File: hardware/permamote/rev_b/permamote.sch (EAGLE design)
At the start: 130 parts, among them J1 TC2030-JLINK-NL, J5 MICRO_USB_B_HIROSE_ZX62R-B-5P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, Q1 PMDXB950UPEL, Q10 PMDXB950UPEL, Q2 PMDXB950UPEL, Q3 PMDXB950UPEL, Q4 PMDXB950UPEL, Q5 PMDXB950UPEL, Q6 PMDXB950UPEL, Q7 PMDXB950UPEL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

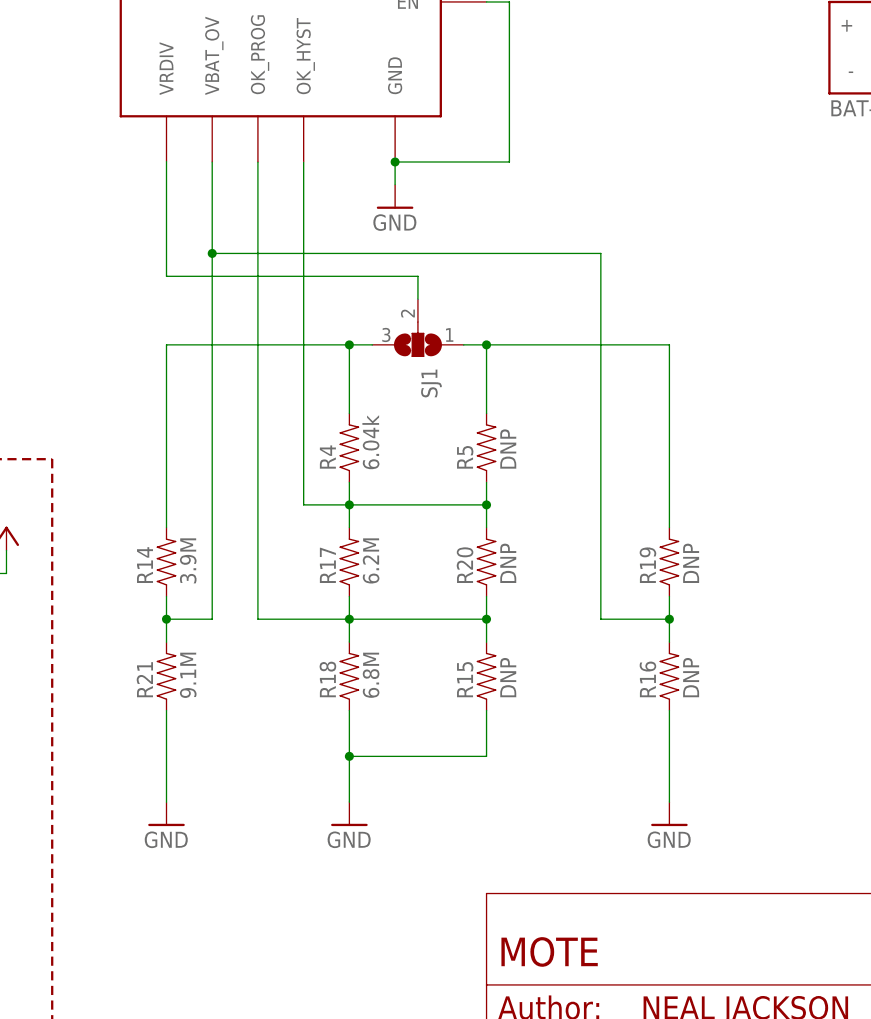
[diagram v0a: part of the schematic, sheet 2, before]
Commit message: Move coin cell holder out from under PIR
Move button/led to debug edge of board
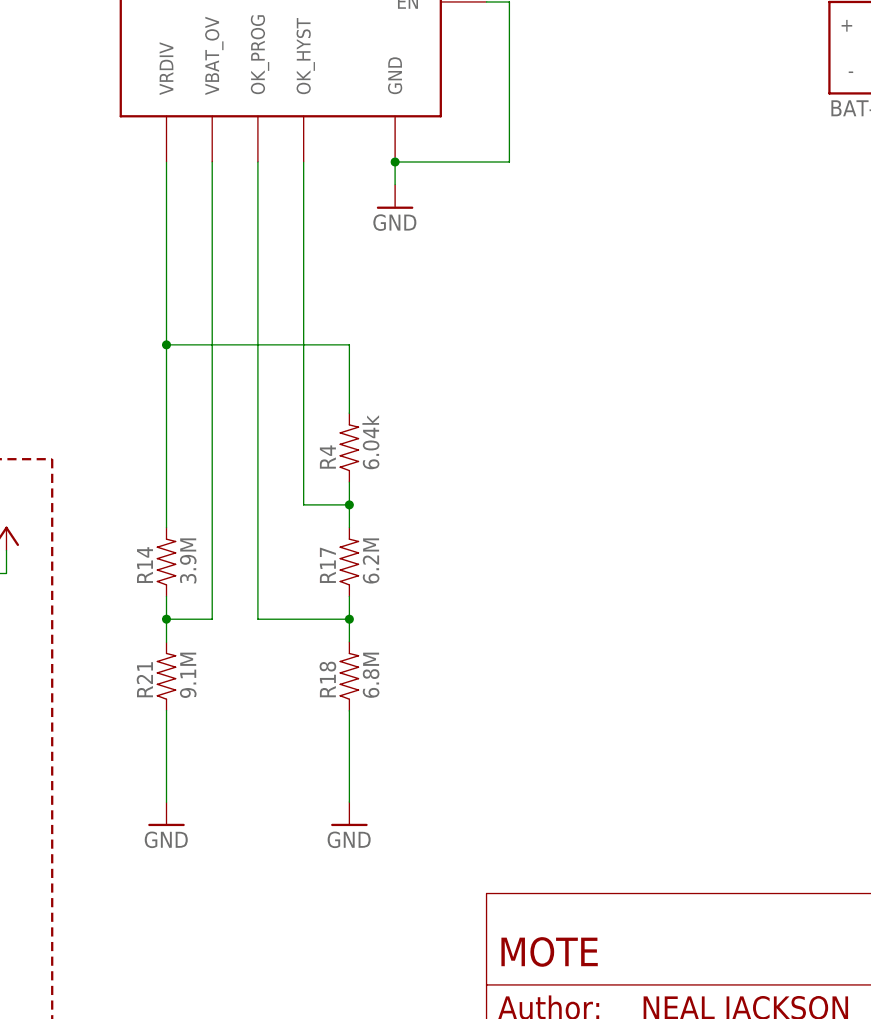
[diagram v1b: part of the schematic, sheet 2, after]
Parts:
- removed R15, R16, R19, R20, R5: DNP, passives:RESISTOR0402_RES
- removed SJ1: (no value), jumper:SJ2W
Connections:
- removed net N$1: R14.2, R4.2, SJ1.3
- removed net N$16: R19.2, R5.2, SJ1.1
- net GND: no longer R15.1, R16.1
- net N$18: no longer R16.2, R19.1
- net N$32: now also R14.2, R4.2; no longer SJ1.2
- net N$57: no longer R15.2, R20.1
- net N$58: no longer R20.2, R5.1
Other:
- note removed: "Divider for Other"
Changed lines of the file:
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@@
 <part name="GND23" library="supply1" library_urn="urn:adsk.eagle:library:371" deviceset="GND" device=""/>
 <part name="GND19" library="supply1" library_urn="urn:adsk.eagle:library:371" deviceset="GND" device=""/>
-<part name="SJ1" library="jumper" library_urn="urn:adsk.eagle:library:252" deviceset="SJ2W" device="" package3d_urn="urn:adsk.eagle:package:15474/1"/>
-<part name="R5" library="passives" deviceset="RESISTOR" device="0402_RES" value="DNP">
-<attribute name="DIGIKEY" value="YAG3306CT-ND"/>
-</part>
-<part name="R20" library="passives" deviceset="RESISTOR" device="0402_RES" value="DNP">
-<attribute name="DIGIKEY" value="YAG3306CT-ND"/>
-</part>
-<part name="R15" library="passives" deviceset="RESISTOR" device="0402_RES" value="DNP">
-<attribute name="DIGIKEY" value="YAG3306CT-ND"/>
-</part>
 <part name="BT2" library="batteries" deviceset="BAT-HLD-002-THM" device="">
 <attribute name="DIGIKEY" value="BAT-HLD-001-THM-ND"/>
@@
 <attribute name="MPN" value="BAT-HLD-001-THM"/>
 </part>
-<part name="R19" library="passives" deviceset="RESISTOR" device="0402_RES" value="DNP">
-<attribute name="DIGIKEY" value="YAG3306CT-ND"/>
-</part>
-<part name="R16" library="passives" deviceset="RESISTOR" device="0402_RES" value="DNP">
-<attribute name="DIGIKEY" value="YAG3306CT-ND"/>
-</part>
-<part name="GND31" library="supply1" library_urn="urn:adsk.eagle:library:371" deviceset="GND" device=""/>
 <part name="L3" library="passives" deviceset="INDUCTOR" device="IHL" value="1uH">
 <attribute name="DIGIKEY" value="541-1319-1-ND"/>
@@
 <text x="2.54" y="66.04" size="2.54" layer="97">Boost Regulator</text>
 <text x="124.46" y="53.34" size="1.778" layer="98" rot="R90" align="bottom-center">Divider for Lithium Titanate</text>
-<text x="162.56" y="53.34" size="1.778" layer="98" rot="R90" align="bottom-center">Divider for Other</text>
 </plain>
 <instances>
@@
 <instance part="GND23" gate="1" x="142.24" y="96.52"/>
 <instance part="GND19" gate="1" x="215.9" y="134.62"/>
-<instance part="SJ1" gate="G$1" x="144.78" y="81.28" rot="R270"/>
-<instance part="R5" gate="G$1" x="152.4" y="71.12" rot="R90">
-<attribute name="DIGIKEY" x="152.4" y="71.12" size="1.778" layer="96" rot="R90" display="off"/>
-</instance>
-<instance part="R20" gate="G$1" x="152.4" y="58.42" rot="R90">
-<attribute name="DIGIKEY" x="152.4" y="58.42" size="1.778" layer="96" rot="R90" display="off"/>
-</instance>
-<instance part="R15" gate="G$1" x="152.4" y="45.72" rot="R90">
-<attribute name="DIGIKEY" x="152.4" y="45.72" size="1.778" layer="96" rot="R90" display="off"/>
-</instance>
 <instance part="BT2" gate="G$1" x="193.04" y="114.3">
 <attribute name="MPN" x="193.04" y="114.3" size="1.778" layer="96" display="off"/>
@@
 <attribute name="MPN" x="215.9" y="114.3" size="1.778" layer="96" display="off"/>
 </instance>
-<instance part="R19" gate="G$1" x="172.72" y="58.42" rot="R90">
-<attribute name="DIGIKEY" x="172.72" y="58.42" size="1.778" layer="96" rot="R90" display="off"/>
-</instance>
-<instance part="R16" gate="G$1" x="172.72" y="45.72" rot="R90">
-<attribute name="DIGIKEY" x="172.72" y="45.72" size="1.778" layer="96" rot="R90" display="off"/>
-</instance>
-<instance part="GND31" gate="1" x="172.72" y="27.94"/>
 <instance part="L3" gate="G$1" x="48.26" y="63.5" rot="R90"/>
 <instance part="GND4" gate="1" x="124.46" y="165.1"/>
@@
 <pinref part="GND22" gate="1" pin="GND"/>
 <pinref part="R18" gate="G$1" pin="1"/>
-<wire x1="137.16" y1="30.48" x2="137.16" y2="35.56" width="0.1524" layer="91"/>
-<pinref part="R15" gate="G$1" pin="1"/>
-<wire x1="137.16" y1="35.56" x2="137.16" y2="40.64" width="0.1524" layer="91"/>
-<wire x1="152.4" y1="40.64" x2="152.4" y2="35.56" width="0.1524" layer="91"/>
-<wire x1="152.4" y1="35.56" x2="137.16" y2="35.56" width="0.1524" layer="91"/>
-<junction x="137.16" y="35.56"/>
+<wire x1="137.16" y1="30.48" x2="137.16" y2="40.64" width="0.1524" layer="91"/>
 </segment>
 <segment>
@@
 <pinref part="BT1" gate="G$1" pin="-"/>
 <wire x1="215.9" y1="137.16" x2="215.9" y2="139.7" width="0.1524" layer="91"/>
-</segment>
-<segment>
-<pinref part="GND31" gate="1" pin="GND"/>
-<pinref part="R16" gate="G$1" pin="1"/>
-<wire x1="172.72" y1="30.48" x2="172.72" y2="40.64" width="0.1524" layer="91"/>
 </segment>
 <segment>
@@
 <junction x="116.84" y="50.8"/>
 <pinref part="U2" gate="G$1" pin="VBAT_OV"/>
-<wire x1="121.92" y1="50.8" x2="121.92" y2="91.44" width="0.1524" layer="91"/>
-<wire x1="121.92" y1="91.44" x2="121.92" y2="101.6" width="0.1524" layer="91"/>
-<wire x1="121.92" y1="91.44" x2="165.1" y2="91.44" width="0.1524" layer="91"/>
-<junction x="121.92" y="91.44"/>
-<wire x1="165.1" y1="91.44" x2="165.1" y2="50.8" width="0.1524" layer="91"/>
-<pinref part="R16" gate="G$1" pin="2"/>
-<pinref part="R19" gate="G$1" pin="1"/>
-<wire x1="172.72" y1="48.26" x2="172.72" y2="50.8" width="0.1524" layer="91"/>
-<wire x1="172.72" y1="50.8" x2="172.72" y2="53.34" width="0.1524" layer="91"/>
-<wire x1="165.1" y1="50.8" x2="172.72" y2="50.8" width="0.1524" layer="91"/>
-<junction x="172.72" y="50.8"/>
+<wire x1="121.92" y1="50.8" x2="121.92" y2="101.6" width="0.1524" layer="91"/>
 </segment>
 </net>
@@
 <segment>
 <pinref part="U2" gate="G$1" pin="VRDIV"/>
-<wire x1="116.84" y1="88.9" x2="116.84" y2="101.6" width="0.1524" layer="91"/>
-<wire x1="116.84" y1="88.9" x2="144.78" y2="88.9" width="0.1524" layer="91"/>
-<pinref part="SJ1" gate="G$1" pin="2"/>
-<wire x1="144.78" y1="88.9" x2="144.78" y2="86.36" width="0.1524" layer="91"/>
+<wire x1="116.84" y1="81.28" x2="116.84" y2="101.6" width="0.1524" layer="91"/>
+<pinref part="R4" gate="G$1" pin="2"/>
+<wire x1="137.16" y1="81.28" x2="137.16" y2="73.66" width="0.1524" layer="91"/>
+<wire x1="137.16" y1="81.28" x2="116.84" y2="81.28" width="0.1524" layer="91"/>
+<pinref part="R14" gate="G$1" pin="2"/>
+<wire x1="116.84" y1="81.28" x2="116.84" y2="60.96" width="0.1524" layer="91"/>
+<junction x="116.84" y="81.28"/>
 </segment>
 </net>
@@
 <wire x1="127" y1="50.8" x2="137.16" y2="50.8" width="0.1524" layer="91"/>
 <junction x="137.16" y="50.8"/>
-<pinref part="R15" gate="G$1" pin="2"/>
-<pinref part="R20" gate="G$1" pin="1"/>
-<wire x1="152.4" y1="48.26" x2="152.4" y2="50.8" width="0.1524" layer="91"/>
-<wire x1="152.4" y1="50.8" x2="152.4" y2="53.34" width="0.1524" layer="91"/>
-<wire x1="137.16" y1="50.8" x2="152.4" y2="50.8" width="0.1524" layer="91"/>
-<junction x="152.4" y="50.8"/>
 </segment>
 </net>
@@
 <wire x1="132.08" y1="63.5" x2="137.16" y2="63.5" width="0.1524" layer="91"/>
 <junction x="137.16" y="63.5"/>
-<pinref part="R20" gate="G$1" pin="2"/>
-<pinref part="R5" gate="G$1" pin="1"/>
-<wire x1="152.4" y1="60.96" x2="152.4" y2="63.5" width="0.1524" layer="91"/>
-<wire x1="152.4" y1="63.5" x2="152.4" y2="66.04" width="0.1524" layer="91"/>
-<wire x1="137.16" y1="63.5" x2="152.4" y2="63.5" width="0.1524" layer="91"/>
-<junction x="152.4" y="63.5"/>
-</segment>
-</net>
-<net name="N$1" class="0">
-<segment>
-<pinref part="SJ1" gate="G$1" pin="3"/>
-<wire x1="139.7" y1="81.28" x2="137.16" y2="81.28" width="0.1524" layer="91"/>
-<pinref part="R4" gate="G$1" pin="2"/>
-<wire x1="137.16" y1="81.28" x2="137.16" y2="73.66" width="0.1524" layer="91"/>
-<wire x1="137.16" y1="81.28" x2="116.84" y2="81.28" width="0.1524" layer="91"/>
-<junction x="137.16" y="81.28"/>
-<pinref part="R14" gate="G$1" pin="2"/>
-<wire x1="116.84" y1="81.28" x2="116.84" y2="60.96" width="0.1524" layer="91"/>
-</segment>
-</net>
-<net name="N$16" class="0">
-<segment>
-<pinref part="R5" gate="G$1" pin="2"/>
-<wire x1="152.4" y1="73.66" x2="152.4" y2="81.28" width="0.1524" layer="91"/>
-<pinref part="SJ1" gate="G$1" pin="1"/>
-<wire x1="152.4" y1="81.28" x2="149.86" y2="81.28" width="0.1524" layer="91"/>
-<pinref part="R19" gate="G$1" pin="2"/>
-<wire x1="172.72" y1="60.96" x2="172.72" y2="81.28" width="0.1524" layer="91"/>
-<wire x1="172.72" y1="81.28" x2="152.4" y2="81.28" width="0.1524" layer="91"/>
-<junction x="152.4" y="81.28"/>
-</segment>
-</net>
+</segment>
+</net>

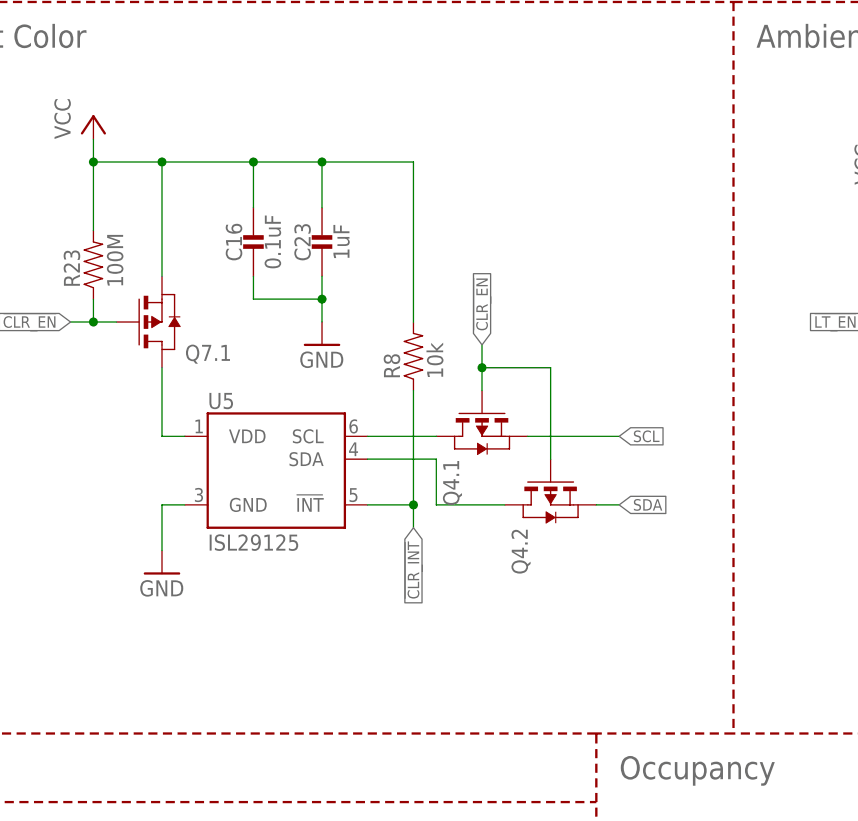
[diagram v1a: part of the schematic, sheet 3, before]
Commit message: Switch to TCS34725 color sensor
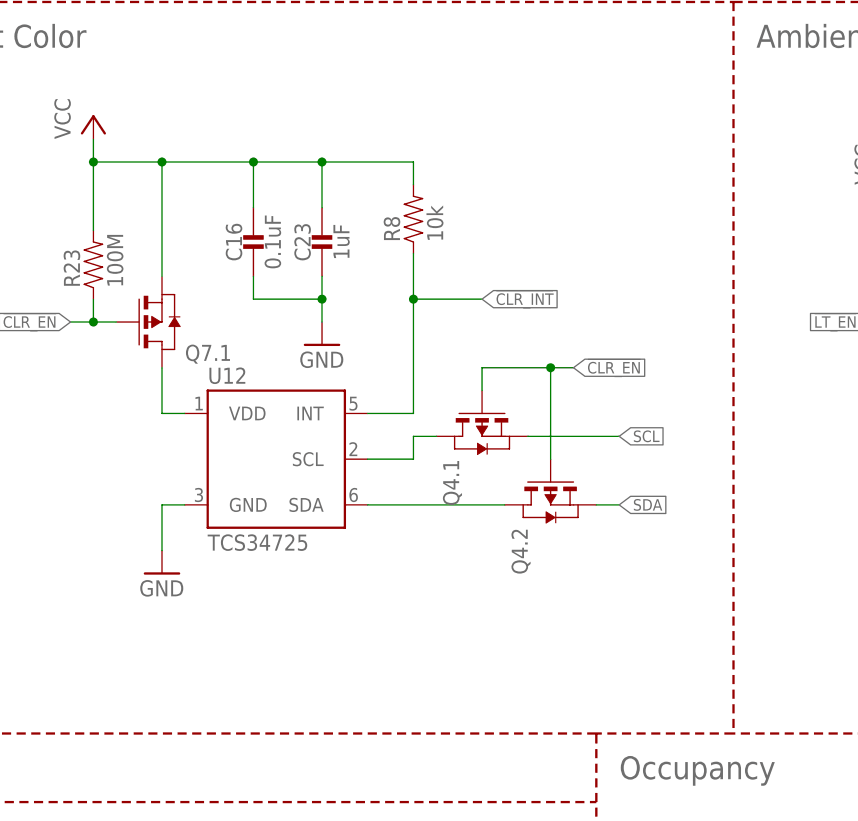
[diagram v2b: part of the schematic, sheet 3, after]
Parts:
- removed U5: ISL29125, chips:ISL29125
- added U12: TCS34725, chips:TCS34725
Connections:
- net !CLR_INT: now also U12.INT; no longer U5.!INT
- net GND: now also U12.GND; no longer U5.GND
- net N$31: now also U12.VDD; no longer U5.VDD
- net N$54: now also U12.SDA; no longer U5.SDA
- net N$55: now also U12.SCL; no longer U5.SCL
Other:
- moved on the sheet: R8
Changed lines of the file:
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@@
 <?xml version="1.0" encoding="utf-8"?>
 <!DOCTYPE eagle SYSTEM "eagle.dtd">
-<eagle version="9.0.0">
+<eagle version="9.0.1">
 <drawing>
 <settings>
@@
 <part name="P+4" library="mote" deviceset="VBAT" device=""/>
 <part name="FRAME3" library="lab11-frames" deviceset="LETTER_L_BLANK" device=""/>
-<part name="U5" library="chips" deviceset="ISL29125" device=""/>
 <part name="U8" library="chips" deviceset="MAX44009" device=""/>
 <part name="C23" library="passives" deviceset="CAPACITOR" device="0402_CAP" value="1uF">
@@
 <part name="TP26" library="headers" deviceset="TEST-POINT" device=""/>
 <part name="TP27" library="headers" deviceset="TEST-POINT" device=""/>
+<part name="U12" library="chips" deviceset="TCS34725" device=""/>
 </parts>
 <sheets>
@@
 <instance part="FRAME3" gate="G$1" x="0" y="0"/>
 <instance part="FRAME3" gate="G$2" x="152.4" y="0"/>
-<instance part="U5" gate="G$1" x="109.22" y="111.76"/>
 <instance part="U8" gate="G$1" x="195.58" y="111.76"/>
 <instance part="C23" gate="G$1" x="121.92" y="144.78">
@@
 <instance part="GND26" gate="1" x="35.56" y="38.1"/>
 <instance part="GND27" gate="1" x="114.3" y="38.1"/>
-<instance part="R8" gate="G$1" x="132.08" y="132.08" rot="R90">
-<attribute name="DIGIKEY" x="132.08" y="132.08" size="1.778" layer="96" rot="R90" display="off"/>
-<attribute name="MPN" x="132.08" y="132.08" size="1.778" layer="96" rot="R90" display="off"/>
+<instance part="R8" gate="G$1" x="132.08" y="147.32" rot="R90">
+<attribute name="DIGIKEY" x="132.08" y="147.32" size="1.778" layer="96" rot="R90" display="off"/>
+<attribute name="MPN" x="132.08" y="147.32" size="1.778" layer="96" rot="R90" display="off"/>
 </instance>
 <instance part="R9" gate="G$1" x="220.98" y="137.16" rot="R90">
@@
 <instance part="Q8" gate=".2" x="93.98" y="45.72" rot="MR180"/>
 <instance part="Q10" gate=".1" x="180.34" y="50.8" rot="MR180"/>
+<instance part="U12" gate="G$1" x="109.22" y="111.76"/>
 </instances>
 <busses>
@@
 <net name="GND" class="0">
 <segment>
-<pinref part="U5" gate="G$1" pin="GND"/>
-<wire x1="106.68" y1="114.3" x2="104.14" y2="114.3" width="0.1524" layer="91"/>
 <pinref part="GND11" gate="1" pin="GND"/>
 <wire x1="104.14" y1="114.3" x2="104.14" y2="109.22" width="0.1524" layer="91"/>
+<pinref part="U12" gate="G$1" pin="GND"/>
+<wire x1="104.14" y1="114.3" x2="106.68" y2="114.3" width="0.1524" layer="91"/>
 </segment>
 <segment>
@@
 <junction x="121.92" y="152.4"/>
 <pinref part="R8" gate="G$1" pin="2"/>
-<wire x1="132.08" y1="134.62" x2="132.08" y2="152.4" width="0.1524" layer="91"/>
+<wire x1="132.08" y1="149.86" x2="132.08" y2="152.4" width="0.1524" layer="91"/>
 <pinref part="P+6" gate="VCC" pin="VCC"/>
 <wire x1="96.52" y1="154.94" x2="96.52" y2="152.4" width="0.1524" layer="91"/>
@@
 <net name="!CLR_INT" class="0">
 <segment>
-<pinref part="U5" gate="G$1" pin="!INT"/>
-<wire x1="127" y1="114.3" x2="132.08" y2="114.3" width="0.1524" layer="91"/>
-<label x="132.08" y="111.76" size="1.27" layer="95" rot="R270" xref="yes"/>
 <pinref part="R8" gate="G$1" pin="1"/>
-<wire x1="132.08" y1="114.3" x2="132.08" y2="111.76" width="0.1524" layer="91"/>
-<wire x1="132.08" y1="127" x2="132.08" y2="114.3" width="0.1524" layer="91"/>
-<junction x="132.08" y="114.3"/>
+<wire x1="132.08" y1="142.24" x2="132.08" y2="137.16" width="0.1524" layer="91"/>
+<pinref part="U12" gate="G$1" pin="INT"/>
+<wire x1="132.08" y1="137.16" x2="132.08" y2="124.46" width="0.1524" layer="91"/>
+<wire x1="127" y1="124.46" x2="132.08" y2="124.46" width="0.1524" layer="91"/>
+<wire x1="132.08" y1="137.16" x2="139.7" y2="137.16" width="0.1524" layer="91"/>
+<junction x="132.08" y="137.16"/>
+<label x="139.7" y="137.16" size="1.27" layer="95" xref="yes"/>
 </segment>
 </net>
@@
 <wire x1="139.7" y1="129.54" x2="147.32" y2="129.54" width="0.1524" layer="91"/>
 <wire x1="147.32" y1="129.54" x2="147.32" y2="119.38" width="0.1524" layer="91"/>
-<wire x1="139.7" y1="129.54" x2="139.7" y2="132.08" width="0.1524" layer="91"/>
-<junction x="139.7" y="129.54"/>
-<label x="139.7" y="132.08" size="1.27" layer="95" rot="R90" xref="yes"/>
+<label x="149.86" y="129.54" size="1.27" layer="95" xref="yes"/>
+<wire x1="147.32" y1="129.54" x2="149.86" y2="129.54" width="0.1524" layer="91"/>
+<junction x="147.32" y="129.54"/>
 </segment>
 </net>
@@
 <net name="N$31" class="0">
 <segment>
-<pinref part="U5" gate="G$1" pin="VDD"/>
-<wire x1="106.68" y1="121.92" x2="104.14" y2="121.92" width="0.1524" layer="91"/>
-<wire x1="104.14" y1="121.92" x2="104.14" y2="129.54" width="0.1524" layer="91"/>
+<wire x1="104.14" y1="124.46" x2="104.14" y2="129.54" width="0.1524" layer="91"/>
 <pinref part="Q7" gate=".1" pin="D"/>
+<pinref part="U12" gate="G$1" pin="VDD"/>
+<wire x1="104.14" y1="124.46" x2="106.68" y2="124.46" width="0.1524" layer="91"/>
 </segment>
 </net>
@@
 <net name="N$54" class="0">
 <segment>
-<wire x1="134.62" y1="119.38" x2="134.62" y2="114.3" width="0.1524" layer="91"/>
 <pinref part="Q4" gate=".2" pin="D"/>
-<wire x1="134.62" y1="114.3" x2="142.24" y2="114.3" width="0.1524" layer="91"/>
-<pinref part="U5" gate="G$1" pin="SDA"/>
-<wire x1="127" y1="119.38" x2="134.62" y2="119.38" width="0.1524" layer="91"/>
+<pinref part="U12" gate="G$1" pin="SDA"/>
+<wire x1="127" y1="114.3" x2="142.24" y2="114.3" width="0.1524" layer="91"/>
 </segment>
 </net>
@@
 <segment>
 <pinref part="Q4" gate=".1" pin="D"/>
-<pinref part="U5" gate="G$1" pin="SCL"/>
-<wire x1="127" y1="121.92" x2="134.62" y2="121.92" width="0.1524" layer="91"/>
-</segment>
-</net>
+<pinref part="U12" gate="G$1" pin="SCL"/>
+<wire x1="132.08" y1="121.92" x2="134.62" y2="121.92" width="0.1524" layer="91"/>
+<wire x1="127" y1="119.38" x2="132.08" y2="119.38" width="0.1524" layer="91"/>
+<wire x1="132.08" y1="119.38" x2="132.08" y2="121.92" width="0.1524" layer="91"/>
+</segment>
+</net>
